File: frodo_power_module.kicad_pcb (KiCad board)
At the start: 2 copper layers, 96.2 x 69 mm, 76 parts, among them J1 Keystone 1048, J10 SWD Header, J2 Molex MicroFit 2x3, J3 Molex MicroFit 2x2, J4 Molex MicroFit 2x2, J5 JST-GH, J6 JST-GH, J7 Molex MicroFit 2x3, U1 STM32F042F6Px, U2 L7805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

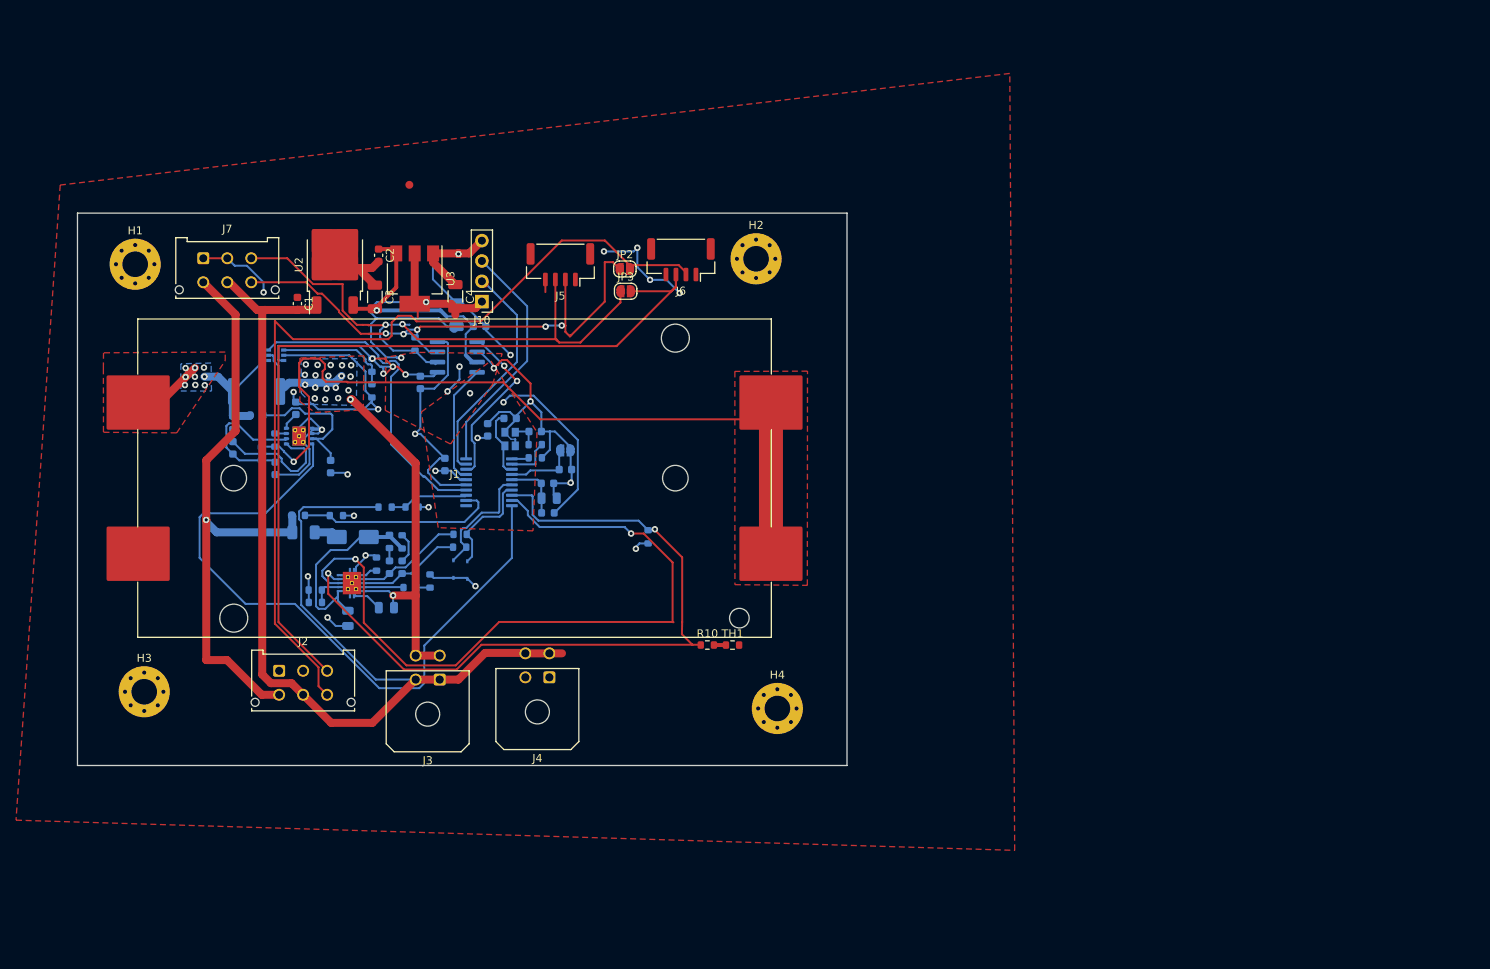
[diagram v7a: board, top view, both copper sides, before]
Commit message: Added Power Traces and made CAN+ and CAN- equal size
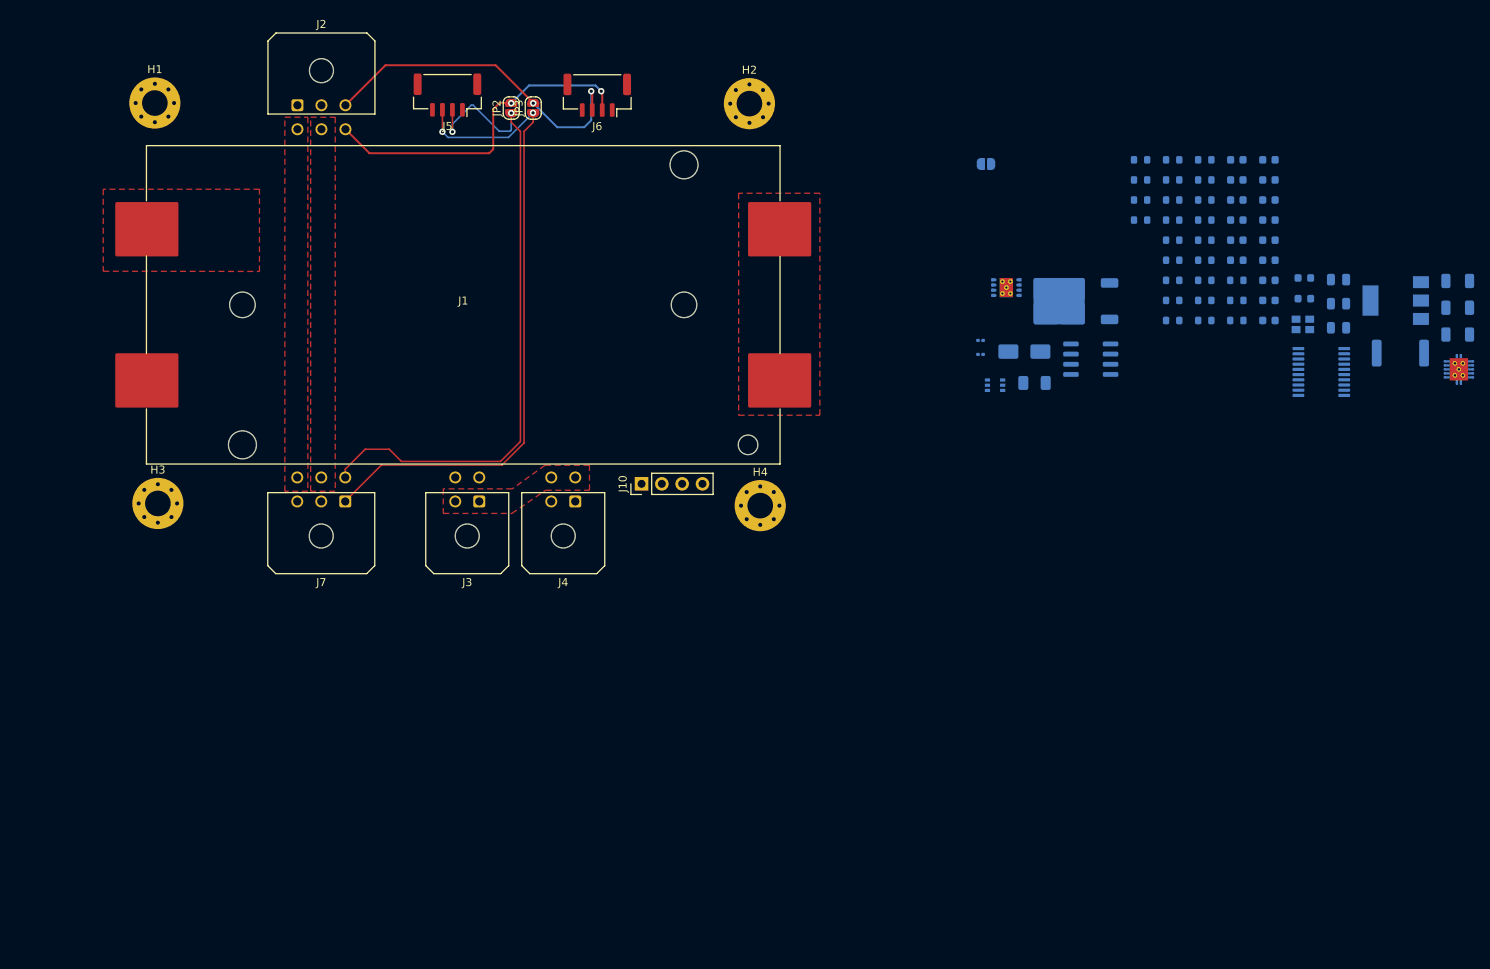
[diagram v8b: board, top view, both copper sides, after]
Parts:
- C1, C2, C3, C4, R10, TH1, U2, U3: moved to B.Cu
- D5, D6: footprint footprints:SOD323F_DIO-L -> Diode_SMD:D_0201_0603Metric
- J2, J7: footprint Connector_Molex:Molex_Micro-Fit_3.0_43045-0612_2x03_P3.00mm_Vertical -> Connector_Molex:Molex_Micro-Fit_3.0_43045-0600_2x03_P3.00mm_Horizontal
- moved R13 143.1 mm to (241.6, 86.0)
- moved U4 140.9 mm to (249.0, 88.0), turned to 180 degrees
- moved C3 135.4 mm to (248.8, 77.0), turned to 180 degrees
- moved C15 130.5 mm to (225.2, 81.9), turned to 180 degrees
- moved C12 129.9 mm to (233.9, 79.8), turned to 180 degrees
- moved C16 126.2 mm to (221.2, 61.8), turned to 180 degrees
- moved C4 125.3 mm to (248.8, 80.3), turned to 180 degrees
- moved C5 125.2 mm to (248.8, 83.7), turned to 180 degrees
- moved C13 124.1 mm to (233.9, 82.8)
- moved C1 122.8 mm to (225.2, 61.8), turned to 180 degrees
- moved U3 122.7 mm to (241.1, 79.4), turned to 180 degrees
- moved R15 122.4 mm to (217.2, 79.4), turned to 180 degrees
- moved R7 121.4 mm to (217.2, 66.8)
- moved C17 121.0 mm to (221.2, 64.3), turned to 180 degrees
- moved R8 121.0 mm to (217.2, 69.4)
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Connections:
- J7 pad 1: GND -> CAN-
- J7 pad 3: CAN- -> GND
- J7 pad 4: VDC -> CAN+
- J7 pad 6: CAN+ -> VDC
- R18 pad 1: Net-(U7-REF) -> Net-(U7-GND)
- R19 pad 2: Net-(U7-REF) -> Net-(U7-GND)
- U7 pad 1: Net-(U7-REF) -> GND
- U7 pad 2: GND -> Net-(U7-GND)
- U7 pad 3: +3V3 -> unconnected-(U7-V+-Pad3)
- U7 pad 4: Net-(J1-Pin_1) -> unconnected-(U7-+-Pad4)
- U7 pad 5: +BATT -> unconnected-(U7---Pad5)
- U7 pad 6: ISENSE -> unconnected-(U7-Pad6)
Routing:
- net GND: track 227.3 -> 0.00 mm, vias 22 -> 0
- net +VSW: track 142.3 -> 0.00 mm
- net +3V3: track 108.3 -> 0.00 mm, vias 12 -> 0
- net Net-(J1-Pin_2): track 102.3 -> 0.00 mm, vias 1 -> 0
- net NTC: track 93.3 -> 0.00 mm, vias 2 -> 0
- net CHARGE_ENABLE: track 90.6 -> 0.00 mm, vias 2 -> 0
- net BLNCR_OUT: track 86.5 -> 0.00 mm
- net VDC: track 75.0 -> 0.00 mm, vias 1 -> 0
- net Net-(J2-Pin_6): track 110.9 -> 42.5 mm, vias 0 -> 2
- net Net-(J2-Pin_3): track 104.8 -> 42.4 mm, vias 0 -> 2
- net +BATT: track 60.7 -> 0.00 mm, vias 20 -> 0
- net ISENSE: track 40.4 -> 0.00 mm
- net +5V: track 32.9 -> 0.00 mm, vias 1 -> 0
- net SWCLK: track 30.2 -> 0.00 mm
- net SWDIO: track 29.4 -> 0.00 mm
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- added copper zone on F.Cu, net +VSW
- added copper zone on F.Cu, net VDC
- removed copper zone on F.Cu, net +3V3
- removed copper zone on B.Cu, net +BATT
- removed copper zone on F.Cu, net +BATT
- removed copper zone on F.Cu, net GND
- removed copper zone on B.Cu, net Net-(J1-Pin_1)
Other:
- board outline removed
